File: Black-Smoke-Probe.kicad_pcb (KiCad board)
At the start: 2 copper layers, 50 x 25 mm, 58 parts, among them J1 Conn_ARM_JTAG_SWD_10, J2 USB_C_Receptacle_USB2.0_14P, J3 MCU_BOOT, J5 MCU_SWD, U1 STM32F103CBUx, U2 74LVC2T45DC, U3 74LVC2T45DC, U4 74LVC2T45DC, U5 USBLC6-2P6, U6 NCP662SQ33, U7 DMG1024UV-7, Y2 8MHz

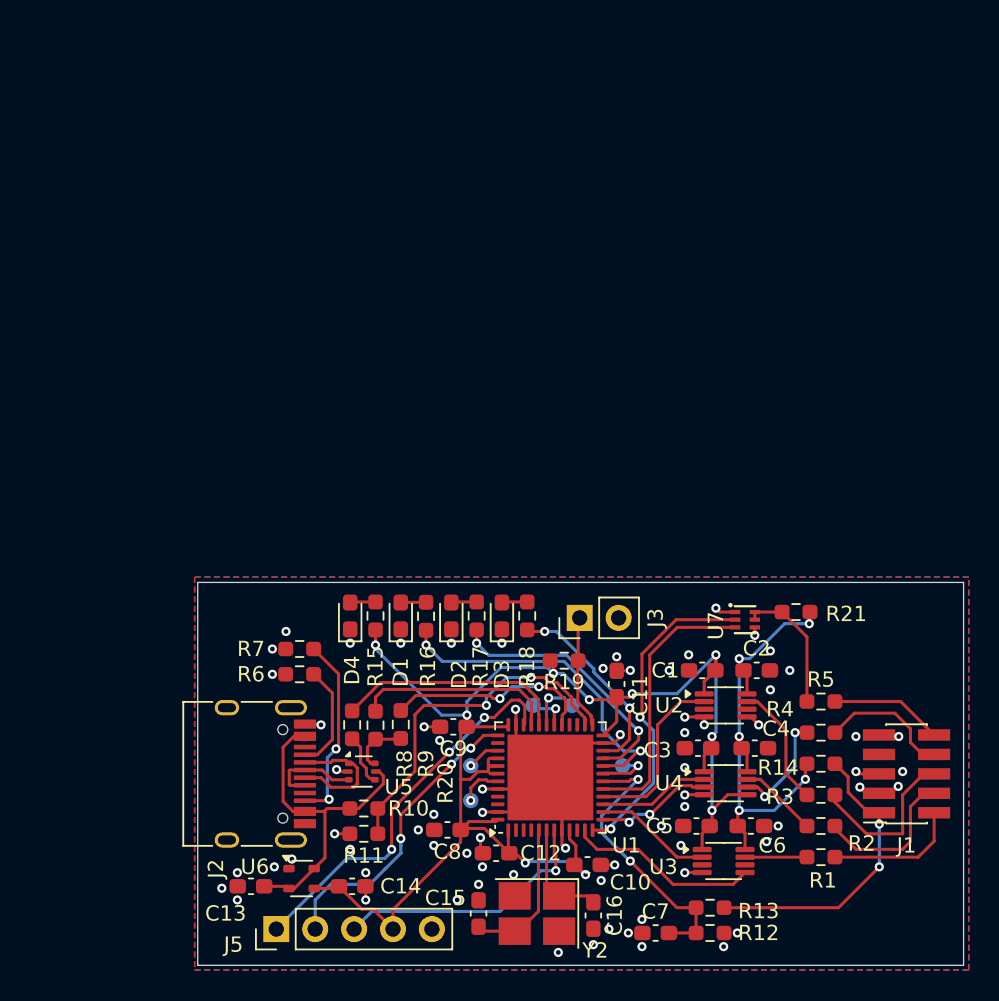
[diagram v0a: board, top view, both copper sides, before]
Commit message: first changes for v1.1
- schematic corrections
- new layout with 4 layer PCB
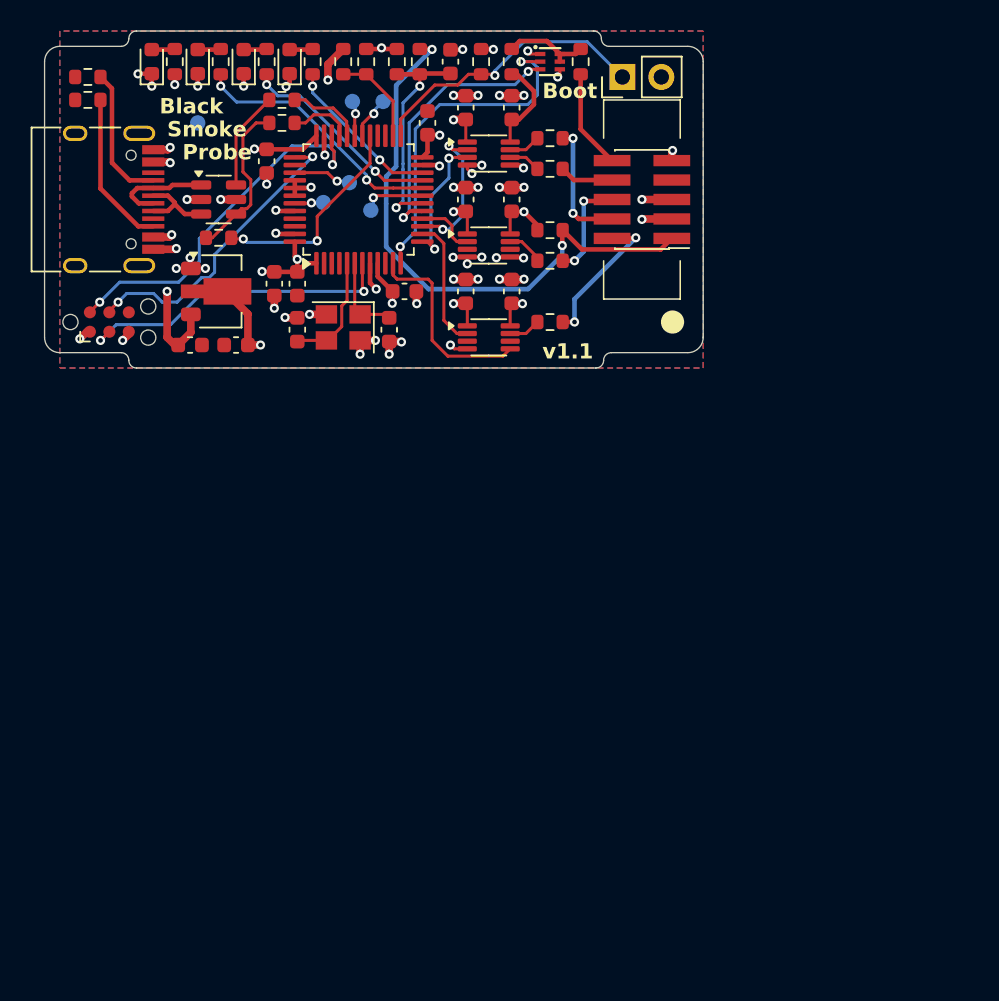
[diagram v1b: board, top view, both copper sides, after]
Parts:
- removed J5: MCU_SWD, Connector_PinHeader_2.54mm:PinHeader_1x05_P2.54mm_Vertical
- removed Y2: 8MHz, Crystal:Crystal_SMD_3225-4Pin_3.2x2.5mm_HandSoldering
- added J4: Conn_ARM_JTAG_SWD_10, Connector_PinHeader_1.27mm:PinHeader_2x05_P1.27mm_Vertical_SMD, F.Cu at (159.0, 80.0)
- added TP6: TestPoint, TestPoint:TestPoint_Pad_D1.0mm, B.Cu at (130.0, 75.0)
- added Y1: 8MHz, Crystal:Crystal_SMD_3225-4Pin_3.2x2.5mm, F.Cu at (139.5, 88.3)
- C1, C3: value 1uF -> 100nF; footprint Capacitor_SMD:C_0603_1608Metric_Pad1.08x0.95mm_HandSolder -> Capacitor_SMD:C_0603_1608Metric
- C10, C11, C12, C13, C14, C6, C8, C9: footprint Capacitor_SMD:C_0603_1608Metric_Pad1.08x0.95mm_HandSolder -> Capacitor_SMD:C_0603_1608Metric
- C15: value 30pF -> 1uF; footprint Capacitor_SMD:C_0603_1608Metric_Pad1.08x0.95mm_HandSolder -> Capacitor_SMD:C_0603_1608Metric
- C16, C7: value 100nF -> 1uF; footprint Capacitor_SMD:C_0603_1608Metric_Pad1.08x0.95mm_HandSolder -> Capacitor_SMD:C_0603_1608Metric
- C2: value 1uF -> 30pF; footprint Capacitor_SMD:C_0603_1608Metric_Pad1.08x0.95mm_HandSolder -> Capacitor_SMD:C_0603_1608Metric
- C4: value 1uF -> 10uF; footprint Capacitor_SMD:C_0603_1608Metric_Pad1.08x0.95mm_HandSolder -> Capacitor_SMD:C_0603_1608Metric
- C5: value 1uF -> 22uF; footprint Capacitor_SMD:C_0603_1608Metric_Pad1.08x0.95mm_HandSolder -> Capacitor_SMD:C_0603_1608Metric
- D1: value RED -> GREEN; footprint LED_SMD:LED_0603_1608Metric_Pad1.05x0.95mm_HandSolder -> LED_SMD:LED_0603_1608Metric
- D2: value ORANGE -> RED; footprint LED_SMD:LED_0603_1608Metric_Pad1.05x0.95mm_HandSolder -> LED_SMD:LED_0603_1608Metric
- D3: value YELLOW -> ORANGE; footprint LED_SMD:LED_0603_1608Metric_Pad1.05x0.95mm_HandSolder -> LED_SMD:LED_0603_1608Metric
- D4: value GREEN -> YELLOW; footprint LED_SMD:LED_0603_1608Metric_Pad1.05x0.95mm_HandSolder -> LED_SMD:LED_0603_1608Metric
- J1: value Conn_ARM_JTAG_SWD_10 -> USB_C_Receptacle_USB2.0_14P; footprint Connector_PinSocket_1.27mm:PinSocket_2x05_P1.27mm_Vertical_SMD -> Connector_USB:USB_C_Receptacle_HRO_TYPE-C-31-M-12
- J2: value USB_C_Receptacle_USB2.0_14P -> MCU_BOOT; footprint Connector_USB:USB_C_Receptacle_HRO_TYPE-C-31-M-12 -> Connector_PinHeader_2.54mm:PinHeader_1x02_P2.54mm_Vertical
- J3: value MCU_BOOT -> SWD_TagConnect; footprint Connector_PinHeader_2.54mm:PinHeader_1x02_P2.54mm_Vertical -> Connector:Tag-Connect_TC2030-IDC-NL_2x03_P1.27mm_Vertical
- R1, R3: value 100 -> 4k7; footprint Resistor_SMD:R_0603_1608Metric_Pad0.98x0.95mm_HandSolder -> Resistor_SMD:R_0603_1608Metric
- R10: value 4k7 -> 22; footprint Resistor_SMD:R_0603_1608Metric_Pad0.98x0.95mm_HandSolder -> Resistor_SMD:R_0603_1608Metric
- R11, R13: value 10k -> 100; footprint Resistor_SMD:R_0603_1608Metric_Pad0.98x0.95mm_HandSolder -> Resistor_SMD:R_0603_1608Metric
- R12: value 4k7 -> 100; footprint Resistor_SMD:R_0603_1608Metric_Pad0.98x0.95mm_HandSolder -> Resistor_SMD:R_0603_1608Metric
- R14, R17, R18, R21, R6, R7, R9: footprint Resistor_SMD:R_0603_1608Metric_Pad0.98x0.95mm_HandSolder -> Resistor_SMD:R_0603_1608Metric
- R15, R16: value 330 -> 100; footprint Resistor_SMD:R_0603_1608Metric_Pad0.98x0.95mm_HandSolder -> Resistor_SMD:R_0603_1608Metric
- R19: value 10k -> 330; footprint Resistor_SMD:R_0603_1608Metric_Pad0.98x0.95mm_HandSolder -> Resistor_SMD:R_0603_1608Metric
- R2, R4, R5: value 100 -> 10k; footprint Resistor_SMD:R_0603_1608Metric_Pad0.98x0.95mm_HandSolder -> Resistor_SMD:R_0603_1608Metric
- R20: value 1k5 -> 330; footprint Resistor_SMD:R_0603_1608Metric_Pad0.98x0.95mm_HandSolder -> Resistor_SMD:R_0603_1608Metric
- R8: value 22 -> 1k5; footprint Resistor_SMD:R_0603_1608Metric_Pad0.98x0.95mm_HandSolder -> Resistor_SMD:R_0603_1608Metric
- TP4: value TestPoint -> TX
- TP5: value TestPoint -> RX
- U1: value STM32F103CBUx -> USBLC6-2SC6; footprint Package_DFN_QFN:QFN-48-1EP_7x7mm_P0.5mm_EP5.6x5.6mm -> Package_TO_SOT_SMD:SOT-23-6
- U2: value 74LVC2T45DC -> AZ1117-3.3; footprint Package_SO:VSSOP-8_2.3x2mm_P0.5mm -> Package_TO_SOT_SMD:SOT-89-3
- U3: value 74LVC2T45DC -> STM32F103CBTx; footprint Package_SO:VSSOP-8_2.3x2mm_P0.5mm -> Package_QFP:LQFP-48_7x7mm_P0.5mm
- U5: value USBLC6-2P6 -> 74LVC2T45DC; footprint Package_TO_SOT_SMD:SOT-666 -> Package_SO:VSSOP-8_2.3x2mm_P0.5mm
- U6: value NCP662SQ33 -> 74LVC2T45DC; footprint Package_TO_SOT_SMD:SC-82AB -> Package_SO:VSSOP-8_2.3x2mm_P0.5mm
- moved J1 65.1 mm to (123.0, 80.0), turned to -90 degrees
- moved R1 60.6 mm to (139.5, 71.0), turned to -90 degrees
- moved R2 58.1 mm to (141.0, 71.0), turned to 90 degrees
- moved C7 54.9 mm to (145.0, 75.0), turned to 90 degrees
- moved R3 54.6 mm to (144.5, 71.0), turned to -90 degrees
- moved C6 53.7 mm to (134.5, 77.5), turned to -90 degrees
- moved R11 52.4 mm to (155.0, 71.0), turned to -90 degrees
- moved C14 51.9 mm to (150.5, 74.0), turned to 90 degrees
- moved R4 51.8 mm to (143.0, 71.0), turned to 90 degrees
- moved J2 51.8 mm to (157.7, 72.0), turned to 90 degrees
- moved R12 51.3 mm to (153.0, 76.0), turned to 0 degrees
- moved U3 49.3 mm to (140.5, 80.0), turned to 90 degrees
- moved R5 47.3 mm to (148.5, 71.0), turned to -90 degrees
- moved C15 46.7 mm to (150.5, 80.0)
- moved C4 45.3 mm to (129.5, 89.5)
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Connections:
- C1 pad 1: +3V3 -> Net-(U3-PB0)
- C13 pad 1: +5V -> +3V3
- C14 pad 1: +3V3 -> Net-(U4-VCCB)
- C15 pad 1: Net-(U1-PD0) -> Net-(U4-VCCB)
- C16 pad 1: GND -> Net-(U4-VCCB)
- C16 pad 2: Net-(U1-PD1) -> GND
- C2 pad 1: Net-(U2-VCCB) -> Net-(U3-PD0)
- C3 pad 1: +3V3 -> GND
- C3 pad 2: GND -> Net-(U3-PD1)
- C4 pad 1: Net-(U2-VCCB) -> +5V
- C6 pad 1: Net-(U2-VCCB) -> +3V3
- C7 pad 1: Net-(U1-PB0) -> +3V3
- J3 pad 1: Net-(J3-Pin_1) -> +3V3
- J3 pad 2: GND -> /SWDIO
- R1 pad 1: Net-(U3-1B) -> +5V
- R1 pad 2: Net-(J1-SWDIO/TMS) -> Net-(U3-PB13)
- R10 pad 1: +5V -> /USBX2+
- R10 pad 2: Net-(U1-PB13) -> /USBX1+
- R11 pad 1: Net-(U1-PB13) -> /RESET
- R11 pad 2: GND -> Net-(J4-~{RESET})
- R12 pad 1: /VREF -> Net-(U4-1B)
- R12 pad 2: Net-(U1-PB0) -> Net-(J4-SWCLK/TCK)
- R13 pad 1: Net-(U1-PB0) -> Net-(U6-1B)
- R13 pad 2: GND -> Net-(J4-SWDIO/TMS)
- R14 pad 1: Net-(U2-VCCB) -> Net-(U5-1B)
- R14 pad 2: /VREF -> Net-(J4-SWO/TDO)
- R15 pad 1: +3V3 -> Net-(U4-2B)
- R15 pad 2: Net-(D4-A) -> Net-(J4-NC/TDI)
- R16 pad 1: /LED0 -> Net-(U4-VCCB)
- R16 pad 2: Net-(D1-A) -> /VREF
- R17 pad 1: /LED1 -> +3V3
- R17 pad 2: Net-(D2-A) -> Net-(D1-A)
- R18 pad 1: /LED2 -> /LED0
- R18 pad 2: Net-(D3-A) -> Net-(D2-A)
- R19 pad 1: +3V3 -> /LED1
- R19 pad 2: Net-(J3-Pin_1) -> Net-(D3-A)
- R2 pad 1: Net-(U4-1B) -> Net-(U3-PB13)
- R2 pad 2: Net-(J1-SWCLK/TCK) -> GND
- R20 pad 1: Net-(U1-PA8) -> /LED2
- R20 pad 2: /USBX1+ -> Net-(D4-A)
- R21 pad 1: Net-(U2-VCCB) -> Net-(U4-VCCB)
- R3 pad 1: Net-(U2-1B) -> /VREF
- R3 pad 2: Net-(J1-SWO/TDO) -> Net-(U3-PB0)
- R4 pad 1: Net-(U4-2B) -> Net-(U3-PB0)
- R4 pad 2: Net-(J1-NC/TDI) -> GND
- R5 pad 1: /RESET -> +3V3
- R5 pad 2: Net-(J1-~{RESET}) -> Net-(J2-Pin_1)
- R6 pad 1: Net-(J2-CC1) -> Net-(J1-CC1)
- R7 pad 1: Net-(J2-CC2) -> Net-(J1-CC2)
- R8 pad 1: /USBX2- -> Net-(U3-PA8)
- R8 pad 2: /USBX1- -> /USBX1+
- R9 pad 1: /USBX2+ -> /USBX2-
- R9 pad 2: /USBX1+ -> /USBX1-
- TP1 pad 1: Net-(U1-PB1) -> Net-(U3-PB1)
- TP2 pad 1: Net-(U1-PB3) -> Net-(U3-PB3)
- TP3 pad 1: Net-(U1-PB7) -> Net-(U3-PB7)
- TP4 pad 1: Net-(U1-PA9) -> /TX
- TP5 pad 1: Net-(U1-PA10) -> /RX
- U1 pad 1: +3V3 -> Net-(J1-D--PadA7)
- U1 pad 2: unconnected-(U1-PC13-Pad2) -> GND
- U1 pad 3: unconnected-(U1-PC14-Pad3) -> Net-(J1-D+-PadA6)
- U1 pad 4: unconnected-(U1-PC15-Pad4) -> /USBX1+
- U1 pad 5: Net-(U1-PD0) -> +5V
- U1 pad 6: Net-(U1-PD1) -> /USBX1-
- U2 pad 1: +3V3 -> GND
- U2 pad 2: Net-(U1-PA6) -> +3V3
- U2 pad 3: unconnected-(U2-2A-Pad3) -> +5V
- U3 pad 2: Net-(U1-PA4) -> unconnected-(U3-PC13-Pad2)
- U3 pad 4: GND -> unconnected-(U3-PC15-Pad4)
- U3 pad 5: Net-(U1-PA1) -> Net-(U3-PD0)
- U3 pad 6: unconnected-(U3-2B-Pad6) -> Net-(U3-PD1)
- U3 pad 7: Net-(U3-1B) -> /NRST
- U3 pad 8: Net-(U2-VCCB) -> GND
- U4 pad 2: Net-(U1-PA5) -> Net-(U3-PA5)
- U4 pad 3: Net-(U1-PA3) -> Net-(U3-PA3)
- U4 pad 8: Net-(U2-VCCB) -> Net-(U4-VCCB)
- U5 pad 1: Net-(J2-D--PadA7) -> +3V3
- U5 pad 2: GND -> Net-(U3-PA6)
- U5 pad 3: Net-(J2-D+-PadA6) -> unconnected-(U5-2A-Pad3)
- U5 pad 4: /USBX1- -> GND
- U5 pad 5: +5V -> GND
- U5 pad 6: /USBX1+ -> unconnected-(U5-2B-Pad6)
- U6 pad 1: GND -> +3V3
- U6 pad 2: +5V -> Net-(U3-PA4)
- U6 pad 3: +3V3 -> unconnected-(U6-2A-Pad3)
- U6 pad 4: +5V -> GND
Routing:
- net +3V3: track 101.3 -> 38.6 mm, vias 10 -> 14
- net Net-(U2-VCCB): track 28.5 -> 0.00 mm, vias 5 -> 0
- net Net-(U4-VCCB): track 0.00 -> 25.7 mm, vias 0 -> 2
- net Net-(J5-Pin_1): track 25.4 -> 0.00 mm, vias 3 -> 0
- net /SWDIO: track 0.00 -> 24.4 mm, vias 0 -> 2
- net Net-(U1-PB13): track 23.0 -> 0.00 mm, vias 2 -> 0
- net /SWCLK: track 0.00 -> 19.9 mm, vias 0 -> 2
- net Net-(J5-Pin_2): track 19.7 -> 0.00 mm, vias 3 -> 0
- net Net-(J2-Pin_1): track 0.00 -> 19.1 mm, vias 0 -> 1
- net /VREF: track 19.6 -> 38.1 mm
- net Net-(U1-PB0): track 18.4 -> 0.00 mm, vias 2 -> 0
- net Net-(U3-PB0): track 0.00 -> 14.8 mm, vias 0 -> 2
- net Net-(U3-PA8): track 0.00 -> 14.1 mm, vias 0 -> 2
- net Net-(U1-PA8): track 13.6 -> 0.00 mm, vias 2 -> 0
- net +5V: track 21.8 -> 35.2 mm, vias 0 -> 5
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- added copper zone on In1.Cu, net +3V3
- added copper zone on In2.Cu, net GND
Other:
- board size 50 x 25 mm -> 43 x 22 mm
- copper layers 2 -> 4
- board text added: "@casartar 2025"
- board text added: "Black"
- board text added: "Boot"
- board text added: "GND"
- board text added: "Probe"
- board text added: "RX"
- board text added: "Smoke"
- board text added: "TX"
- board text added: "v1.1"

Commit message: bom, schematic, drc corrections and add logo
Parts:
- moved C10 0.20 mm to (134.8, 85.5)
- moved C9 0.20 mm to (136.3, 85.5)
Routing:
- net GND: track 48.9 -> 51.4 mm, vias 53 -> 56
- net Net-(U3-PA5): track 9.35 -> 10.2 mm
- net Net-(U4-VCCB): track 25.7 -> 26.5 mm, vias 2 -> 3

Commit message: corrections
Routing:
- net +3V3: track 38.6 -> 41.2 mm

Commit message: corrections
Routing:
- net +3V3: track 41.2 -> 40.3 mm
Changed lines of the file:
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@@
 	)
 	(segment
-		(start 144.6625 77.25)
-		(end 143.85 77.25)
-		(width 0.3)
-		(layer "F.Cu")
-		(net 6)
-	)
-	(segment
 		(start 136.3375 79.75)
 		(end 136.3375 78.75)
@@
 		(min_thickness 0.25)
 		(filled_areas_thickness no)
-		(fill yes
+		(fill
 			(thermal_gap 0.5)
 			(thermal_bridge_width 0.5)
@@
 		(polygon
 			(pts
-				(xy 121 91) (xy 163 91) (xy 163 69) (xy 121 69)
+				(xy 120 91) (xy 163 91) (xy 163 69) (xy 120 69)
 			)
 		)

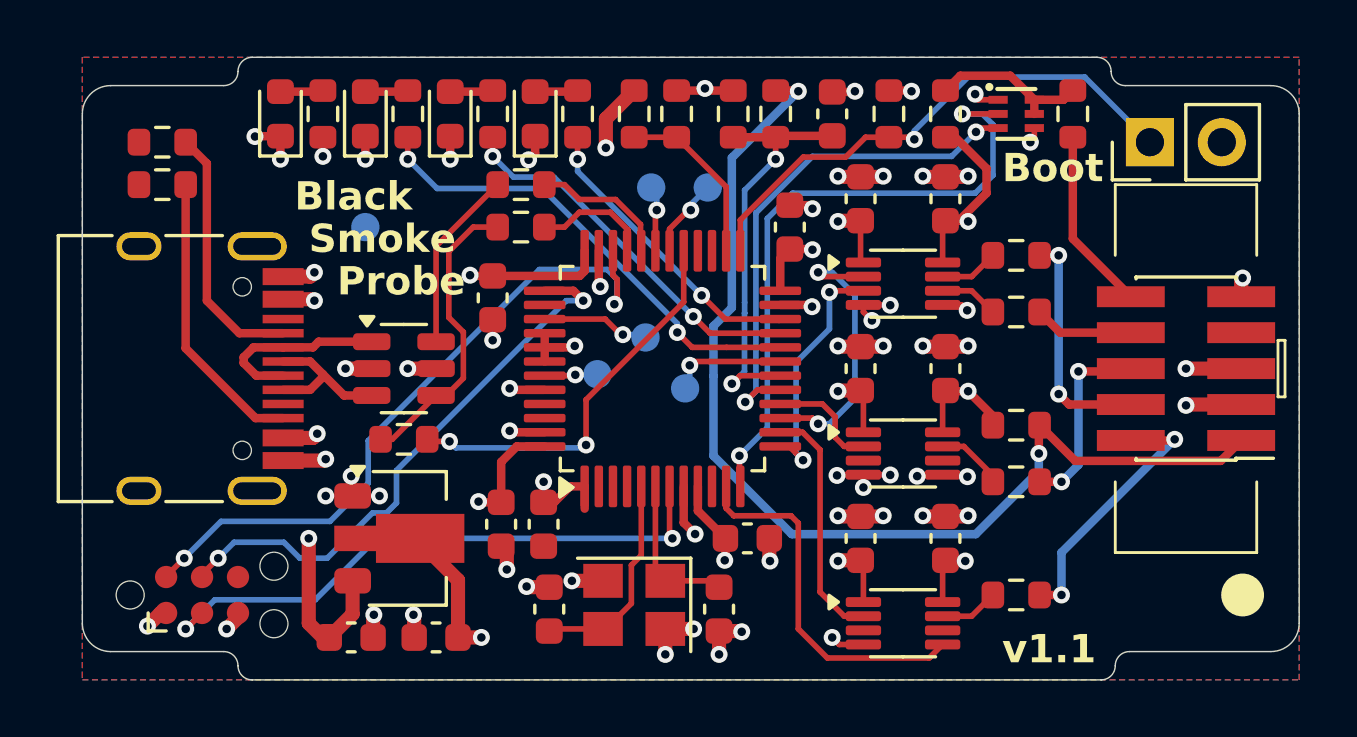
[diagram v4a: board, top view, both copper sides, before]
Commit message: remove top gnd plane
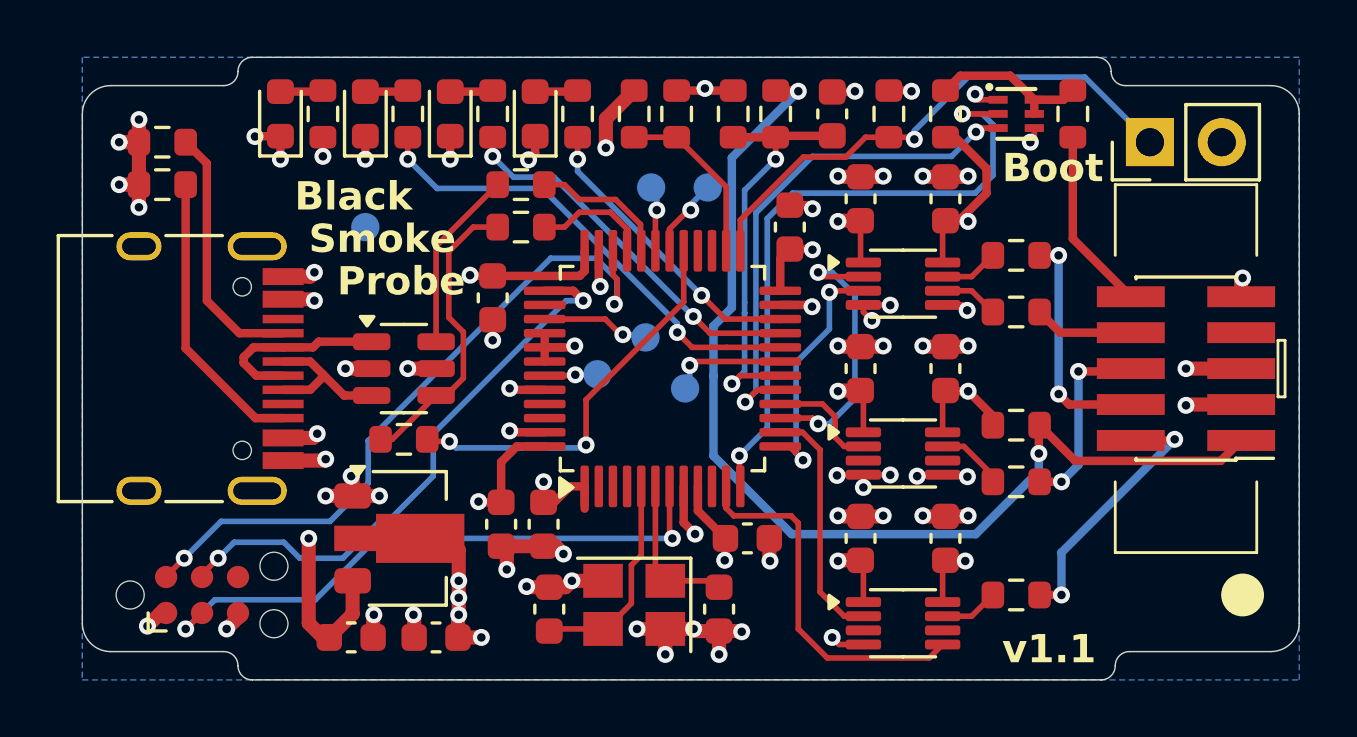
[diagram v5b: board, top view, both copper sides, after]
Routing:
- net GND: track 51.4 -> 63.7 mm, vias 56 -> 62
- net +3V3: track 40.3 -> 37.7 mm, vias 14 -> 17
- removed copper zone on F.Cu, net GND

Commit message: v1.1.1 changed capacitor from 100nf to 30pf
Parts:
- C3: value 100nF -> 30pF
